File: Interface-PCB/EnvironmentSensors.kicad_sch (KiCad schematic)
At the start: 30 parts, among them IC1 SN74LVC245AN, J10 LEVEL_SENSOR, J11 TEMPERATURE_SENSOR, J12 TEMPERATURE_SENSOR, J5 LEVEL_SENSOR, J6 LEVEL_SENSOR, J7 LEVEL_SENSOR, J8 LEVEL_SENSOR, J9 LEVEL_SENSOR

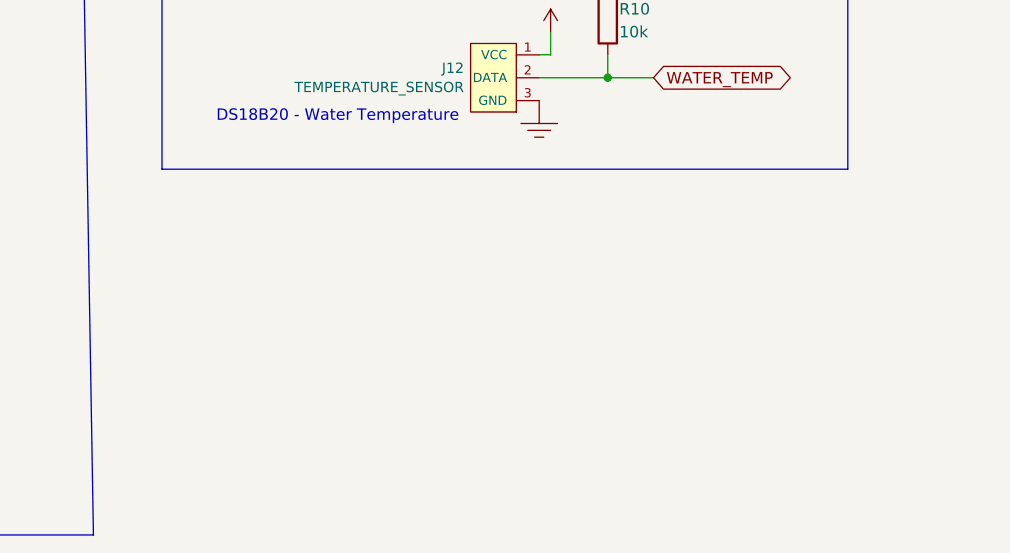
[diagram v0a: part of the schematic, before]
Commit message: Add silkscreen and logos to PCB
Complete silkscreen layer on PCB
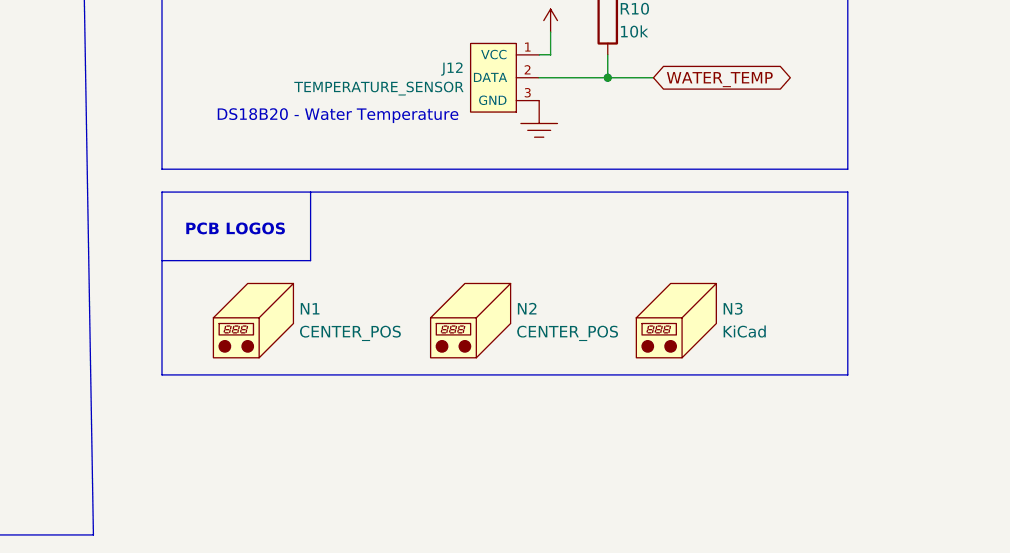
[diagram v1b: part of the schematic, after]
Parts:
- added N1, N2: CENTER_POS, AA_Custom_Components:Polarity_Center_Positive_7.5mm_SilkScreen, symbol Mechanical:Housing
- added N3: KiCad, Symbol:KiCad-Logo2_8mm_SilkScreen, symbol Mechanical:Housing
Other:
- note added: "PCB LOGOS"
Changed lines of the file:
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@@
+    (stroke (width 0) (type default) (color 0 0 0 0))
+  )
+  (polyline (pts (xy 111.76 152.4) (xy 111.76 132.08))
+    (stroke (width 0) (type default) (color 0 0 0 0))
+  )
+  (polyline (pts (xy 111.76 132.08) (xy 187.96 132.08))
     (stroke (width 0) (type default) (color 0 0 0 0))
   )
@@
     (stroke (width 0) (type default) (color 0 0 0 0))
   )
+  (polyline (pts (xy 187.96 132.08) (xy 187.96 152.4))
+    (stroke (width 0) (type default) (color 0 0 0 0))
+  )
+  (polyline (pts (xy 187.96 152.4) (xy 111.76 152.4))
+    (stroke (width 0) (type default) (color 0 0 0 0))
+  )
   (wire (pts (xy 45.72 74.93) (xy 45.72 77.47))
     (stroke (width 0) (type default) (color 0 0 0 0))
@@
     (stroke (width 0) (type default) (color 0 0 0 0))
   )
+  (polyline (pts (xy 128.27 139.7) (xy 128.27 132.08))
+    (stroke (width 0) (type default) (color 0 0 0 0))
+  )
   (wire (pts (xy 90.17 80.01) (xy 91.44 80.01))
     (stroke (width 0) (type default) (color 0 0 0 0))
@@
   )
   (polyline (pts (xy 15.24 95.25) (xy 16.51 170.18))
+    (stroke (width 0) (type default) (color 0 0 0 0))
+  )
+  (polyline (pts (xy 111.76 139.7) (xy 128.27 139.7))
     (stroke (width 0) (type default) (color 0 0 0 0))
   )
@@
   (text "Water Level" (at 20.32 41.91 0)
     (effects (font (size 1.27 1.27)) (justify left bottom))
+  )
+  (text "PCB LOGOS" (at 114.3 137.16 0)
+    (effects (font (size 1.27 1.27) (thickness 0.254) bold) (justify left bottom))
   )
   (text "LEVEL SHIFTING" (at 115.57 20.32 0)
@@
     (pin "2")
   )
+  (symbol (lib_id "Mechanical:Housing") (at 123.19 146.05 0) (unit 1)
+    (in_bom yes) (on_board yes) (fields_autoplaced)
+    (property "Reference" "N1" (id 0) (at 127 145.0974 0)
+      (effects (font (size 1.27 1.27)) (justify left))
+    )
+    (property "Value" "CENTER_POS" (id 1) (at 127 147.6374 0)
+      (effects (font (size 1.27 1.27)) (justify left))
+    )
+    (property "Footprint" "AA_Custom_Components:Polarity_Center_Positive_7.5mm_SilkScreen" (id 2) (at 124.46 144.78 0)
+      (effects (font (size 1.27 1.27)) hide)
+    )
+    (property "Datasheet" "~" (id 3) (at 124.46 144.78 0)
+      (effects (font (size 1.27 1.27)) hide)
+    )
+  )
   (symbol (lib_id "Device:R") (at 184.15 45.72 270) (unit 1)
     (in_bom yes) (on_board yes)
@@
     (pin "1")
   )
+  (symbol (lib_id "Mechanical:Housing") (at 147.32 146.05 0) (unit 1)
+    (in_bom yes) (on_board yes) (fields_autoplaced)
+    (property "Reference" "N2" (id 0) (at 151.13 145.0974 0)
+      (effects (font (size 1.27 1.27)) (justify left))
+    )
+    (property "Value" "CENTER_POS" (id 1) (at 151.13 147.6374 0)
+      (effects (font (size 1.27 1.27)) (justify left))
+    )
+    (property "Footprint" "AA_Custom_Components:Polarity_Center_Positive_7.5mm_SilkScreen" (id 2) (at 148.59 144.78 0)
+      (effects (font (size 1.27 1.27)) hide)
+    )
+    (property "Datasheet" "~" (id 3) (at 148.59 144.78 0)
+      (effects (font (size 1.27 1.27)) hide)
+    )
+  )
   (symbol (lib_id "Device:R") (at 184.15 66.04 270) (unit 1)
     (in_bom yes) (on_board yes)
@@
     (pin "1")
   )
+  (symbol (lib_id "Mechanical:Housing") (at 170.18 146.05 0) (unit 1)
+    (in_bom yes) (on_board yes) (fields_autoplaced)
+    (property "Reference" "N3" (id 0) (at 173.99 145.0974 0)
+      (effects (font (size 1.27 1.27)) (justify left))
+    )
+    (property "Value" "KiCad" (id 1) (at 173.99 147.6374 0)
+      (effects (font (size 1.27 1.27)) (justify left))
+    )
+    (property "Footprint" "Symbol:KiCad-Logo2_8mm_SilkScreen" (id 2) (at 171.45 144.78 0)
+      (effects (font (size 1.27 1.27)) hide)
+    )
+    (property "Datasheet" "~" (id 3) (at 171.45 144.78 0)
+      (effects (font (size 1.27 1.27)) hide)
+    )
+  )
   (symbol (lib_id "Device:R") (at 184.15 50.8 270) (unit 1)

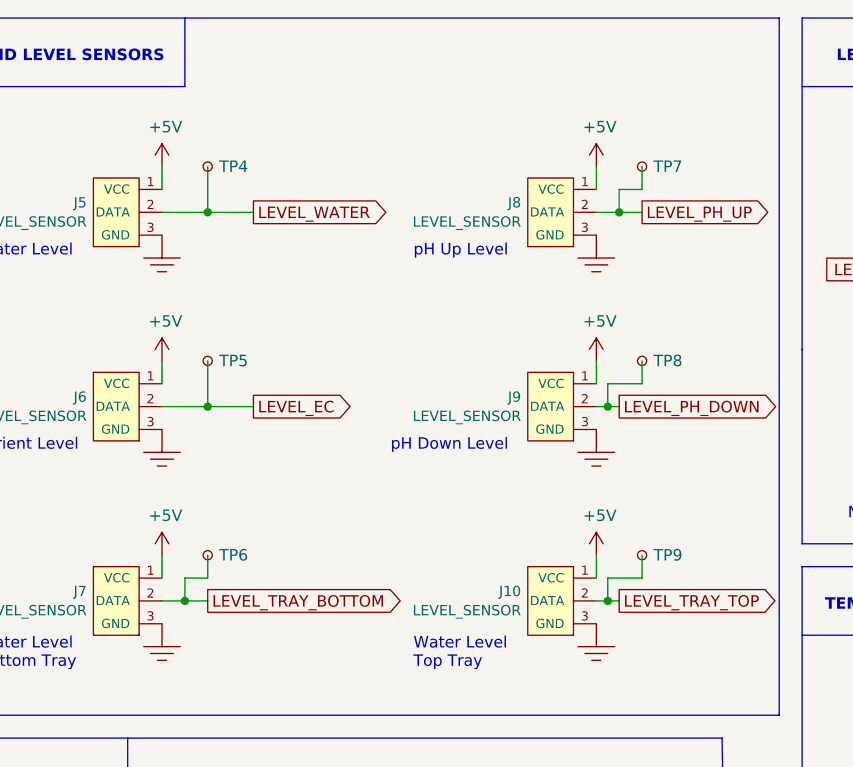
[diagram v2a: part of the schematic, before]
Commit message: Complete PCB routing
- Complete routing of all tracks
- DRC shows no errors, only non-warnings for kicad-buzzard related items
- Remove Level Sensor test points
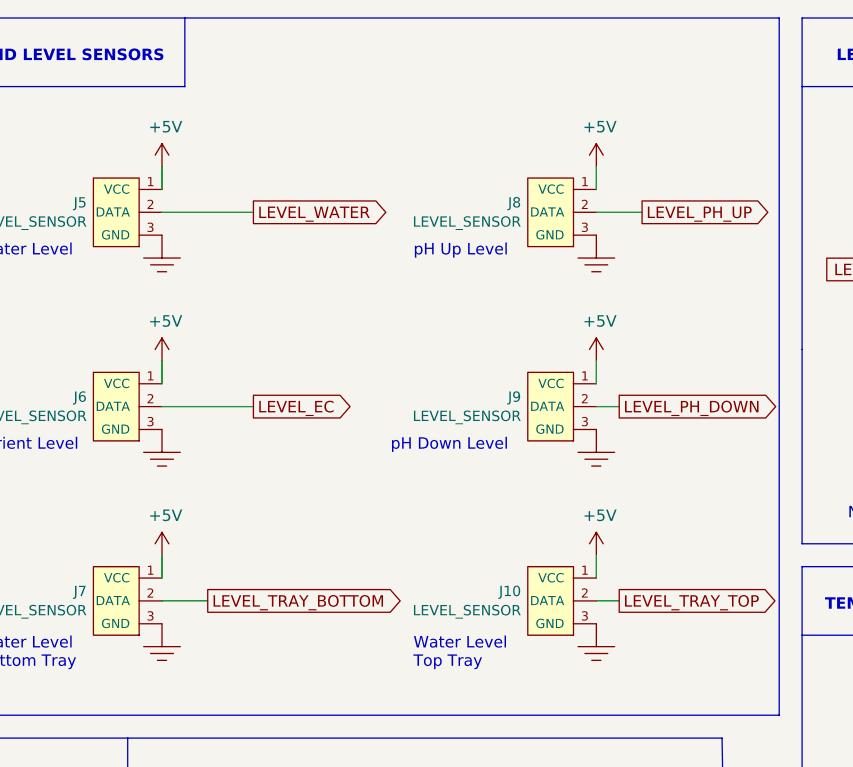
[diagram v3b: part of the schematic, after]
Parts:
- removed TP4, TP5, TP6, TP7, TP8, TP9: PAD, TestPoint:TestPoint_Pad_D1.5mm, symbol Connector:TestPoint_Small

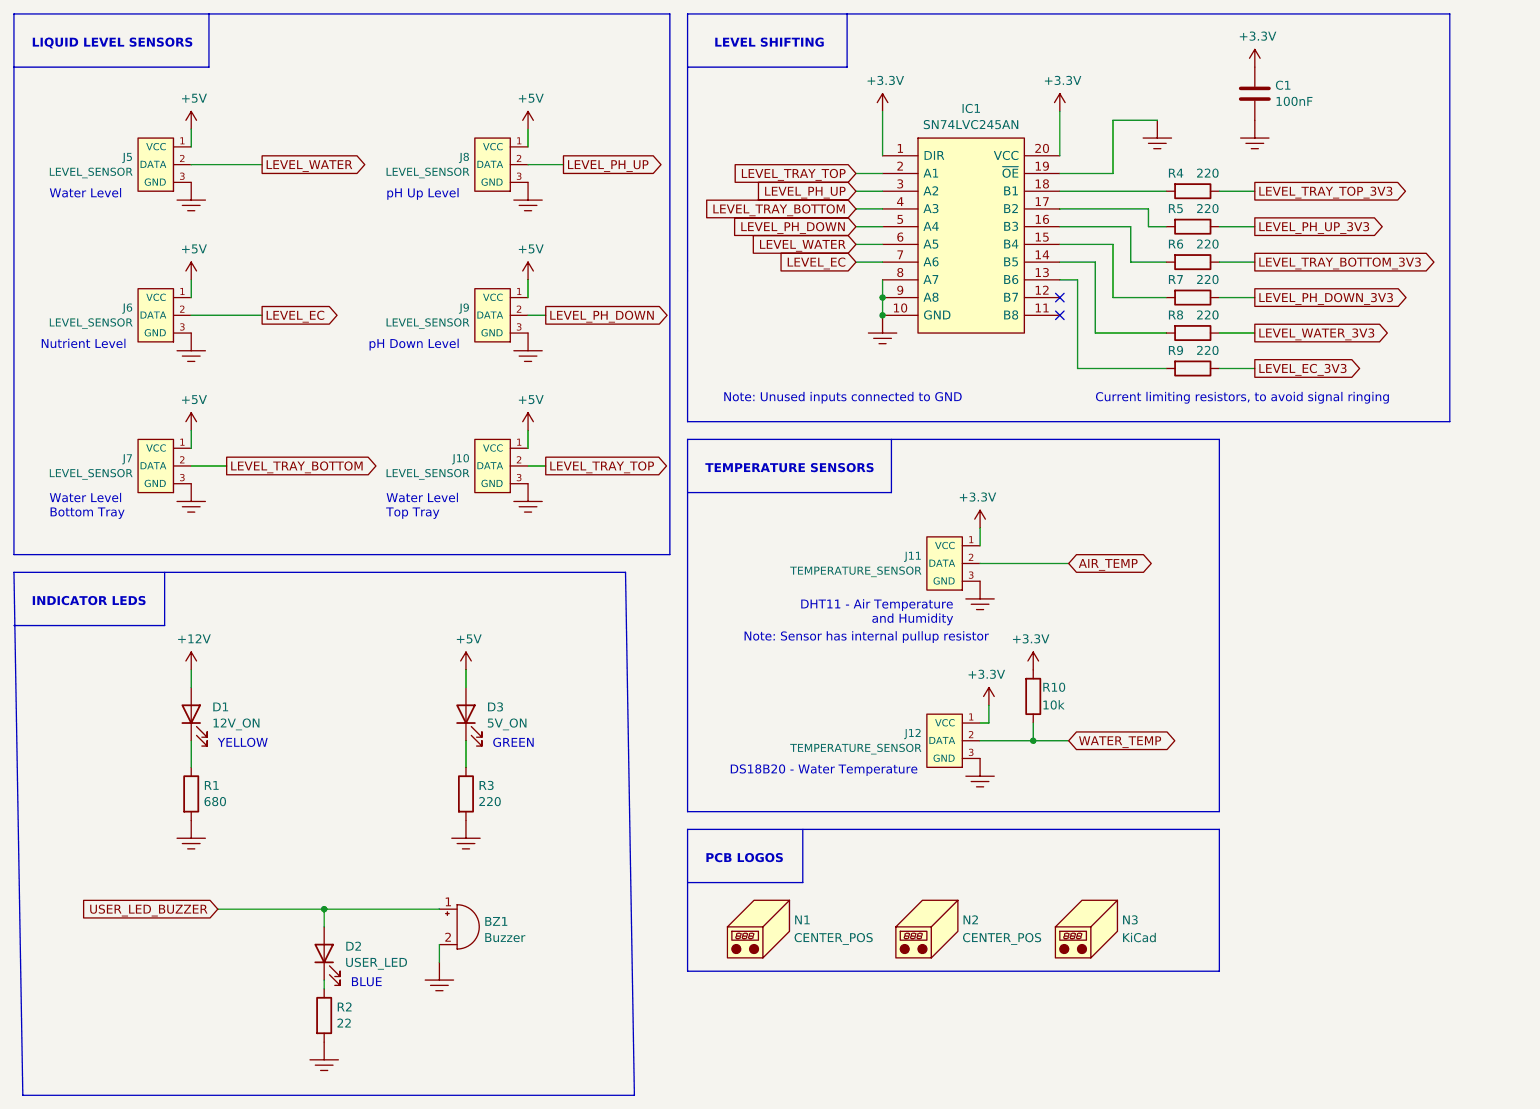
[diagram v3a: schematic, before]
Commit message: Add 3.3V LDO Regulator and Barrel Jack Connectors
- Add mounted barrel jack connectors for 12V and 5V
- Add 5V to 3.3V LDO breakout board
- Adjust silkscreen
- Export and verify Gerbers
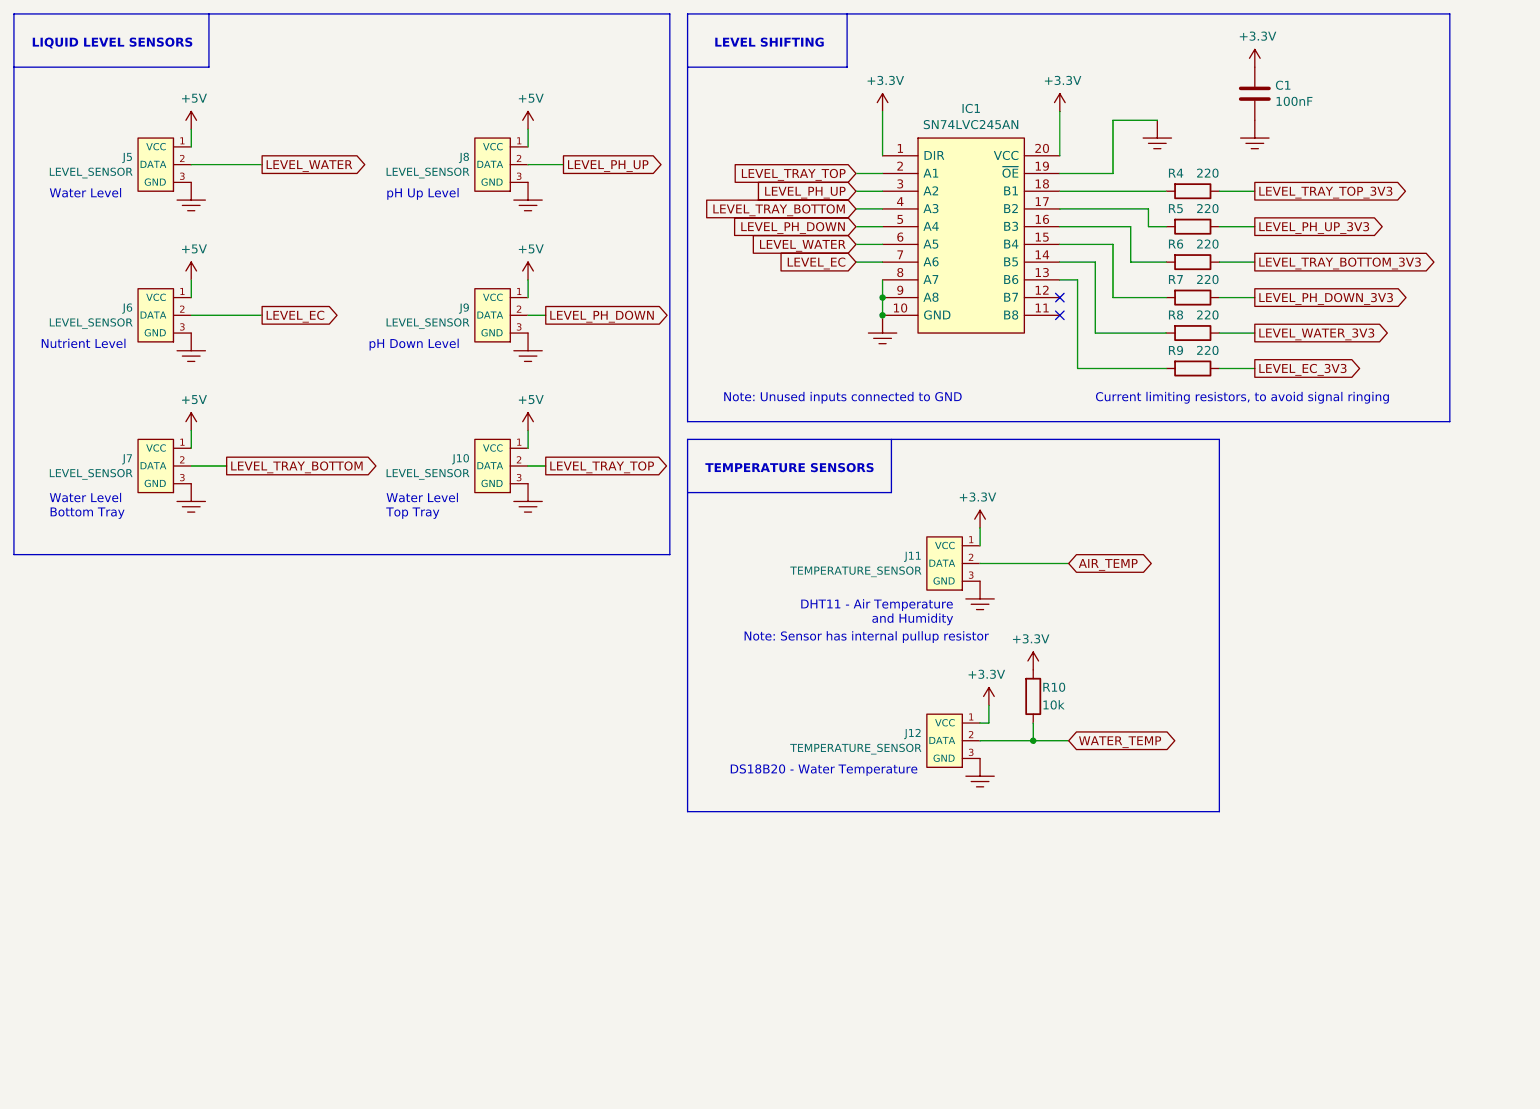
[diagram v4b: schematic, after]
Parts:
- removed BZ1: Buzzer, AA_Custom_Components:Buzzer_Generic_D12.2mm_H6.5mm, symbol Device:Buzzer
- removed D1: 12V_ON, AA_Custom_Components:LED_SS_1206_3216Metric_Pad1.42x1.75mm_HandSolder, symbol Device:LED
- removed D2: USER_LED, AA_Custom_Components:LED_SS_1206_3216Metric_Pad1.42x1.75mm_HandSolder, symbol Device:LED
- removed D3: 5V_ON, AA_Custom_Components:LED_SS_1206_3216Metric_Pad1.42x1.75mm_HandSolder, symbol Device:LED
- removed N1, N2: CENTER_POS, AA_Custom_Components:Polarity_Center_Positive_7.5mm_SilkScreen, symbol Mechanical:Housing
- removed N3: KiCad, Symbol:KiCad-Logo2_8mm_SilkScreen, symbol Mechanical:Housing
- removed R1: 680, AA_Custom_Components:R_SS_Axial_DIN0207_L6.3mm_D2.5mm_P10.16mm_Horizontal, symbol Device:R
- removed R2: 22, AA_Custom_Components:R_SS_Axial_DIN0207_L6.3mm_D2.5mm_P10.16mm_Horizontal, symbol Device:R
- removed R3: 220, AA_Custom_Components:R_SS_Axial_DIN0207_L6.3mm_D2.5mm_P10.16mm_Horizontal, symbol Device:R
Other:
- note removed: "BLUE"
- note removed: "GREEN"
- note removed: "INDICATOR LEDS"
- note removed: "PCB LOGOS"
- note removed: "YELLOW"
